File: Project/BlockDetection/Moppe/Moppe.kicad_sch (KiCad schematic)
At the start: 41 parts, among them J1 Conn_01x02_Pin, J2 Conn_01x02_Pin, J3 Conn_01x02_Pin, J4 Conn_01x02_Pin, J5 Conn_01x02_Pin, J6 Conn_01x02_Pin, J7 Amphenol RJHSE5380, J8 Conn_01x02_Pin, Q1 BC856, Q2 BC856 or BC557, Q3 BC856 or BC557, Q4 BC856 or BC557, U1 PC847, U2 PC817

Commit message: tlp620
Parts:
- added D14: S5AC, Diode_THT:D_DO-201AD_P15.24mm_Horizontal, symbol Diode:1N5400
- added D15: 1N5400, Diode_THT:D_DO-201AD_P15.24mm_Horizontal, symbol Diode:1N5400
- added D16, D17: IR26-21C_L110_TR8, LED_SMD:LED_1206_3216Metric, symbol LED:IR26-21C_L110_TR8
- added J9: Conn_01x03_Socket, Package_TO_SOT_THT:TO-92_Inline, symbol Connector:Conn_01x03_Socket
- added Q5: BC557, Package_TO_SOT_SMD:SOT-23, symbol Transistor_BJT:BC856
- added Q6: BC547, Package_TO_SOT_THT:TO-92_Inline, symbol Transistor_BJT:BC547
- added R11: 10R, symbol Device:R
- added R12: 1K8, symbol Device:R
- added U4: TLP620, Package_SO:SOP-4_4.4x2.6mm_P1.27mm, symbol Isolator:TLP290
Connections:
- new net: D17.1 (K), Q6.1 (C)
- new net: Q5.1 (B), Q6.2 (B), R11.1
- new net: D14.2 (A), D15.1 (K), J9.1 (Pin_1), Q5.2 (E), Q6.3 (E)
- new net: R12.1, U4.1
- new net: D16.1 (K), D17.2 (A), R12.2
- new net: J9.3 (Pin_3), U4.2
- new net: D14.1 (K), D15.2 (A), J9.2 (Pin_2), R11.2
- new net: D16.2 (A), Q5.3 (C)

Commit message: efter test
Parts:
- removed C1, C2, C3, C4: 10 µF, symbol Device:C_Polarized_Small
- removed D13: D_Bridge_+-AA, Module:Pololu_Breakout-16_15.2x20.3mm, symbol Device:D_Bridge_+-AA
- removed D14: S5AC, Diode_THT:D_DO-201AD_P15.24mm_Horizontal, symbol Diode:1N5400
- removed D15: 1N5400, Diode_THT:D_DO-201AD_P15.24mm_Horizontal, symbol Diode:1N5400
- removed D16, D17: IR26-21C_L110_TR8, LED_SMD:LED_1206_3216Metric, symbol LED:IR26-21C_L110_TR8
- removed J7: Amphenol RJHSE5380, Connector_RJ:RJ45_Amphenol_RJHSE5380, symbol Connector:RJ45_Shielded
- removed J8: Conn_01x02_Pin, Connector:Tag-Connect_TC2030-IDC-FP_2x03_P1.27mm_Vertical, symbol Connector:Conn_01x02_Pin
- removed J9: Conn_01x03_Socket, Package_TO_SOT_THT:TO-92_Inline, symbol Connector:Conn_01x03_Socket
- removed Q1: BC856, Package_TO_SOT_SMD:SOT-23, symbol Transistor_BJT:BC856
- removed Q2, Q3, Q4: BC856 or BC557, Package_TO_SOT_SMD:SOT-23, symbol Transistor_BJT:BC856
- removed Q5: BC557, Package_TO_SOT_SMD:SOT-23, symbol Transistor_BJT:BC856
- removed Q6: BC547, Package_TO_SOT_THT:TO-92_Inline, symbol Transistor_BJT:BC547
- removed U2: PC817, Package_DIP:DIP-4_W7.62mm, symbol Isolator:PC817
- removed U4: TLP620, Package_SO:SOP-4_4.4x2.6mm_P1.27mm, symbol Isolator:TLP290
- added C1: 100nF, symbol Device:C
- added C2: 10µF, Package_QFP:LQFP-100_14x14mm_P0.5mm, symbol Device:C_Polarized
- added C3: 3,3µF, Package_QFP:LQFP-100_14x14mm_P0.5mm, symbol Device:C_Polarized
- added J7: Conn_01x04_Socket, Connector:Tag-Connect_TC2030-IDC-NL_2x03_P1.27mm_Vertical, symbol Connector:Conn_01x04_Socket
- added Q1, Q2, Q3, Q4: BC557, Package_TO_SOT_THT:TO-92_Inline, symbol Transistor_BJT:BC557
- added U2: MAX485E, Package_SO:SOIC-8_3.9x4.9mm_P1.27mm, symbol Interface_UART:MAX485E
- added U3: ESP32-C3-WROOM-02, RF_Module:ESP32-C3-WROOM-02, symbol RF_Module:ESP32-C3-WROOM-02
- added U4: LT1129-3.3_SOT223, Package_TO_SOT_SMD:SOT-223-3_TabPin2, symbol Regulator_Linear:LT1129-3.3_SOT223
- R10: value 22R -> 4K7; footprint (none) -> Inductor_THT:L_CommonMode_PulseElectronics_PH9455x105NL_1
- R11: value 10R -> 4K7; footprint (none) -> Inductor_THT:L_CommonMode_PulseElectronics_PH9455x105NL_1
- R12: value 1K8 -> 10K; footprint (none) -> Inductor_THT:L_CommonMode_PulseElectronics_PH9455x105NL_1
- R9: value 470R -> 120R; footprint (none) -> Inductor_THT:L_CommonMode_PulseElectronics_PH9455x105NL_1
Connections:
- net at R11.1: now also R9.2, J7.3 (Pin_3), U2.7 (B)
- net GND: now reaches J1.1 (Pin_1), J2.1 (Pin_1), J4.1 (Pin_1), J5.1 (Pin_1), J6.1 (Pin_1), U1.4, U1.6, U1.8
- net GND: no longer J3.1 (Pin_1), U1.2
- net GNDD: now reaches U1.15
- net GNDD: now also R11.2, R12.2, U1.11, U1.13, U1.9, C1.2, C2.2, C3.2, J7.4 (Pin_4), U2.5 (GND), U3.19 (GND), U3.9 (GND), U4.2 (GND)
- net at U1.16: now also U3.18 (IO0)
- net at D2.2 (A), D3.2 (A), D4.2 (A)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: now also Q2.3 (E), Q3.3 (E), Q4.3 (E); no longer D1.2 (A), D5.1 (K), J1.2 (Pin_2), R10.2, R9.1
- net at R12.1: now also U2.2 (~{RE}), U2.3 (DE)
- net at R5.2: now also Q1.1 (C)
- net at R6.2: now also Q2.1 (C)
- net at R2.1: now also Q2.2 (B)
- net at U1.12: now also U3.16 (IO2)
- net at R10.1: now also C1.1, C2.1, C3.1, U2.8 (VCC), U3.1 (3V3), U3.2 (EN), U4.3 (VO)
- net at R7.2: now also Q3.1 (C)
- net at U1.14: now also U3.17 (IO1)
- net at R3.1: now also Q3.2 (B)
- net at R4.1: now also Q4.2 (B)
- net at U1.10: now also U3.15 (IO3)
- net at R8.2: now also Q4.1 (C)
- net at R1.1: now also Q1.2 (B)
- new net: J3.1 (Pin_1), U1.2
- new net: U2.1 (RO), U3.12 (IO21/TXD)
- new net: U2.4 (DI), U3.11 (IO20/RXD)
- new net: J7.2 (Pin_2), R10.2, R9.1, U2.6 (A)
- new net: D1.2 (A), D5.1 (K), J1.2 (Pin_2), Q1.3 (E)
- new net: J7.1 (Pin_1), U4.1 (VI)
- no-connect marks 0 -> 9
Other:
- moved on the sheet: D10, D11, D12, D2, D3, D4, D6, D7, D8, D9, J2, J3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

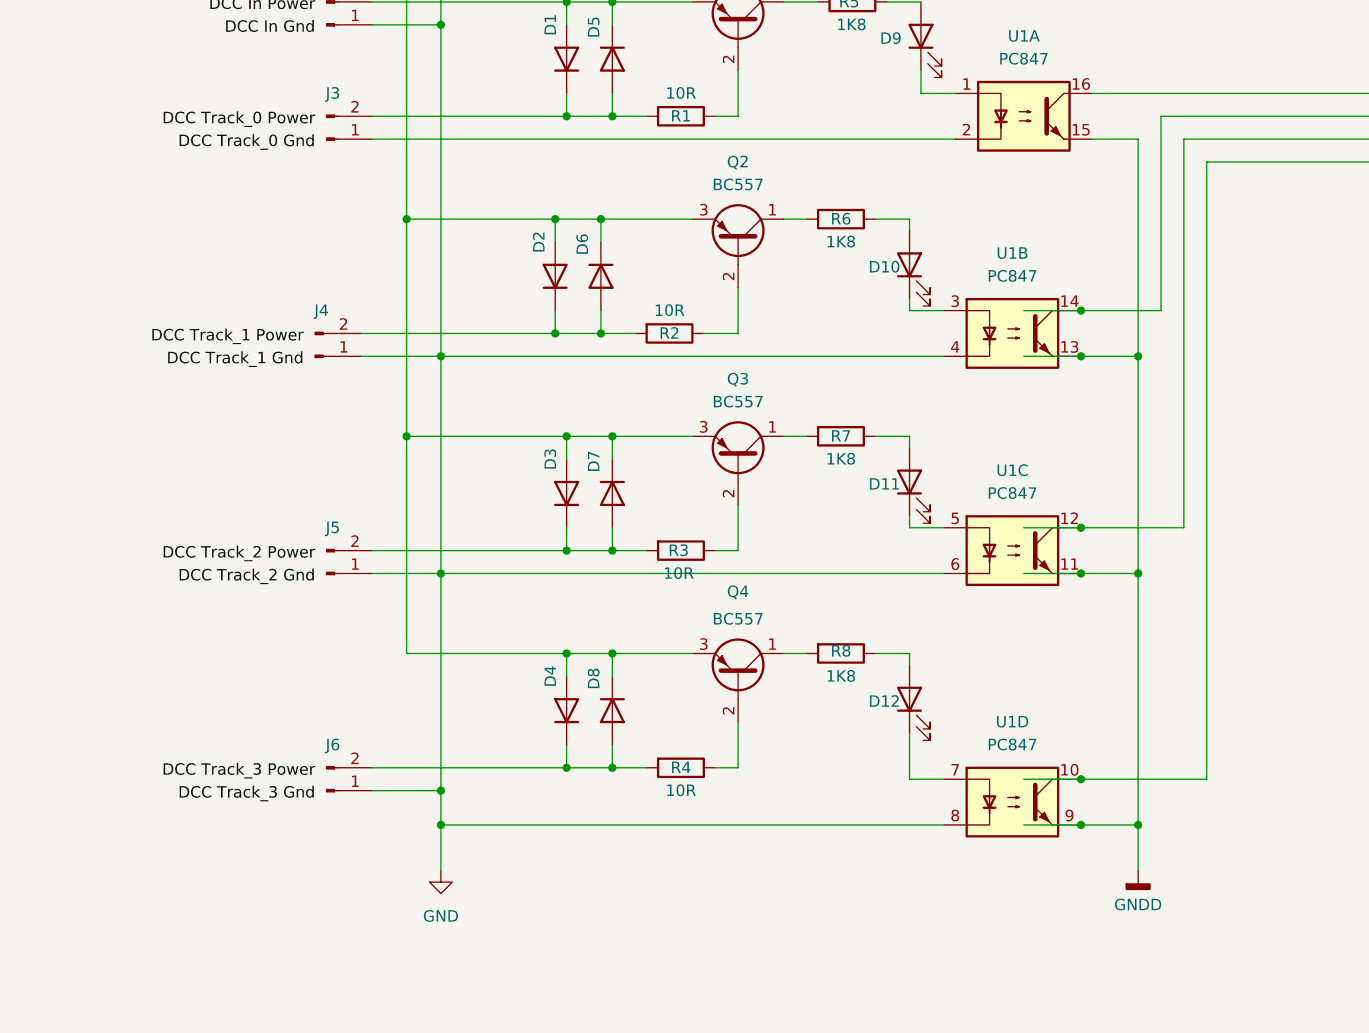
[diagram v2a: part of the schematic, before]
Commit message: AI Help Wifi_On_Off
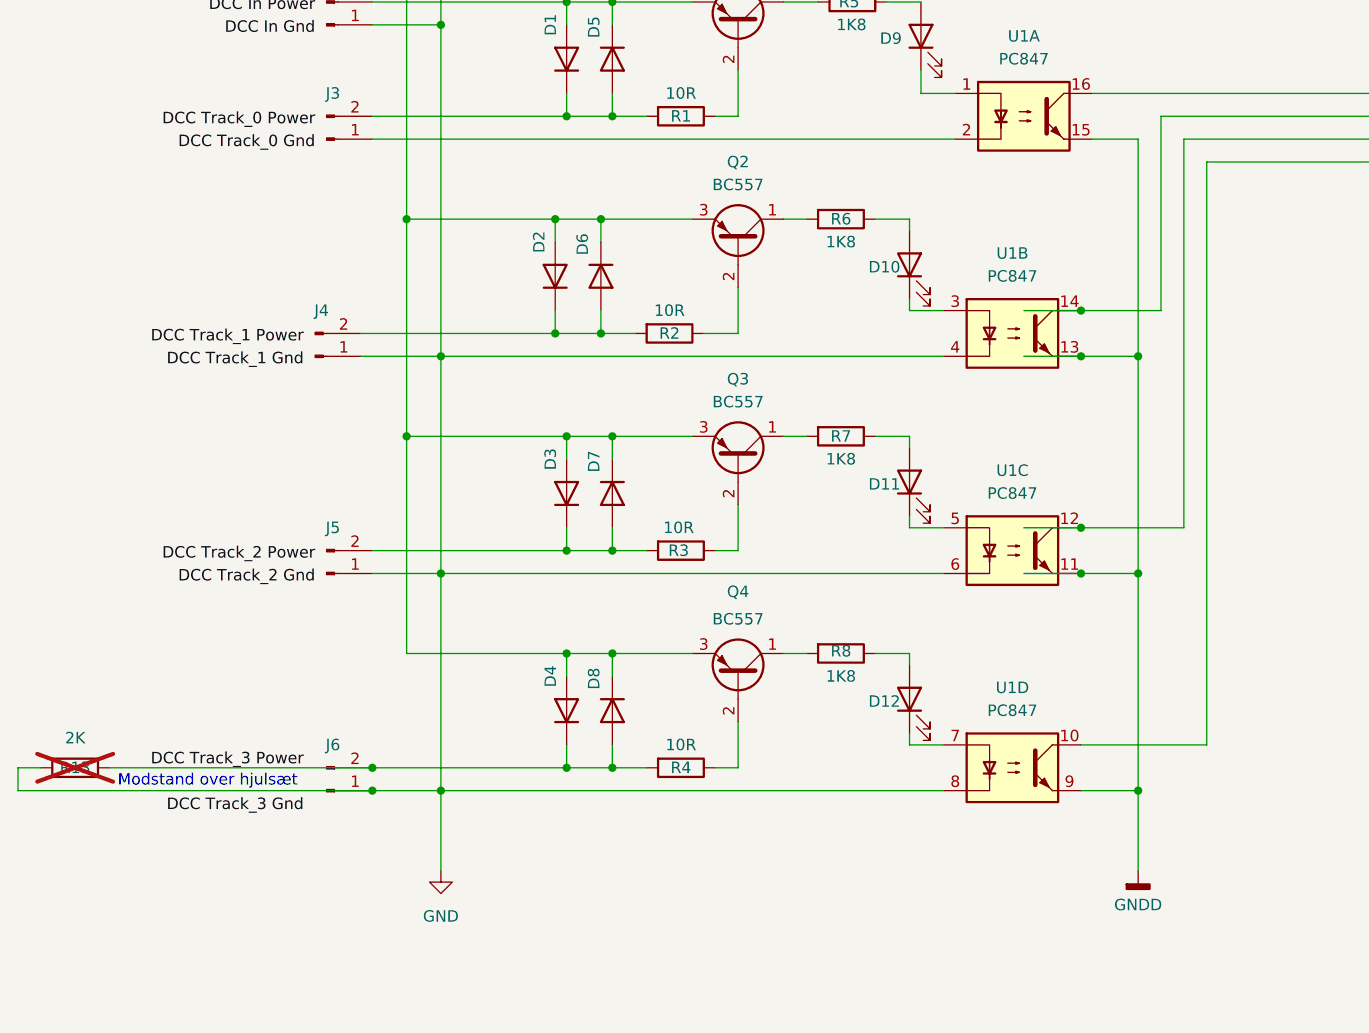
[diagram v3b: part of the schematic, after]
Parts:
- added R13: 2K, symbol Device:R
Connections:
- net DCC Track_3 Power: now also D4.1 (K), D8.2 (A), J6.2 (Pin_2), R4.2, R13.1
- net GND: now also R13.2
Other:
- note added: "Modstand over hjulsæt"
- moved on the sheet: U1D

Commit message: Moppe
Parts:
- added C4, C5, C6, C7: 4;7µF, symbol Device:C_Polarized
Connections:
- net GND: now also C5.2, C6.2, C7.2
- net at D9.1 (K), U1.1: now also C4.1
- net at J3.1 (Pin_1), U1.2: now also C4.2
- net at D11.1 (K), U1.5: now also C6.1
- net at D12.1 (K), U1.7: now also C7.1
- net at D10.1 (K), U1.3: now also C5.1
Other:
- moved on the sheet: D10, D11, D12, D9, R5, U1A, U1B, U1C, U1D

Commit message: SporBesat a la´ Moppe
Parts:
- removed U2: MAX485E, Package_SO:SOIC-8_3.9x4.9mm_P1.27mm, symbol Interface_UART:MAX485E
- added R14, R15: 20K, Inductor_THT:L_CommonMode_PulseElectronics_PH9455x105NL_1, symbol Device:R
- added U5: 4N35, Package_DIP:DIP-6_W7.62mm, symbol Isolator:4N35
- added U6: MAX3485, Package_DIP:DIP-16_W7.62mm, symbol Interface_UART:MAX3485
- C4, C5, C6, C7: value 4;7µF -> 1µF
- R12: value 10K -> 20K
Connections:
- net GNDD: now also U6.5 (GND); no longer R12.2
- net at D9.1 (K), U1.1: no longer C4.1
- net at Q3.1 (C), R7.2: now also C6.1
- net at D11.1 (K), U1.5: no longer C6.1
- net at U3.12 (IO21/TXD): now also R15.2, U6.4 (DI)
- net +3V3: now reaches R12.1
- net +3V3: now also C1.1, C2.1, C3.1, R10.1, U3.1 (3V3), U4.3 (VO), R14.1, R15.1, U6.8 (VCC)
- net at U3.11 (IO20/RXD): now also R12.2, U6.1 (RO)
- net at J7.2 (Pin_2), R10.2, R9.1: now also U6.6 (A)
- net at J7.3 (Pin_3), R11.1, R9.2: now also U6.7 (B)
- net at Q1.1 (C), R5.2: now also C4.1
- net at Q2.1 (C), R6.2: now also C5.1
- net at D12.1 (K), U1.7: no longer C7.1
- net at D10.1 (K), U1.3: no longer C5.1
- net at U3.3 (IO4): now also R14.2, U6.2 (~{RE}), U6.3 (DE)
- net +5V: now reaches J7.1 (Pin_1), U4.1 (VI)
- net at Q4.1 (C), R8.2: now also C7.1
- now unconnected: U3.2 (EN)
- no-connect marks 9 -> 8
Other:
- note added: "For at beregne størrelsen på kondensator C4, C5, C6 & C7, der skal holde strømmen til en LED i 200 mikrosekunder, skal du bruge formlen for elektrisk ladning og strøm: C= (I*t)/(ΔV) Find dine værdier Tid (t): 200 µs = 0,0002 sekunder LED strøm (I): En typisk LED bruger omkring 20 mA, hvilket er 0,02 Ampere. Spændingsfald (Δ V): Det er forskellen på din forsyningsspænding (V_start}) og den mindste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"
- moved on the sheet: C1, C2, C3, C4, C5, C6, C7, D1, D10, D11, D12, D2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

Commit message: Moppe2.svg
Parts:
- removed C4, C5, C6, C7: 1µF, symbol Device:C_Polarized
- added C4, C5, C6, C7: 1µF, symbol Device:C
- added JP1: Jumper_2_Small_Bridged, symbol Jumper:Jumper_2_Small_Bridged
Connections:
- net GND: now also C5.2, C6.2, C7.2
- net at J3.1 (Pin_1), U1.2: now also C4.2
- net at Q3.1 (C), R7.2: now also C6.1
- net at Q1.1 (C), R5.2: now also C4.1
- net at J7.3 (Pin_3), R11.1, U6.7 (B): now also JP1.2 (B); no longer R9.2
- net at Q2.1 (C), R6.2: now also C5.1
- net at Q4.1 (C), R8.2: now also C7.1
- new net: JP1.1 (A), R9.2
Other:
- moved on the sheet: R11

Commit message: moppe rj45
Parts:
- added J8, J9: RJ45, Connector_RJ:RJ45_Amphenol_RJMG1BD3B8K1ANR, symbol Connector:RJ45
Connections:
- net GNDD: now also J8.6, J8.7, J8.8, J9.6, J9.7, J9.8
- net at J7.3 (Pin_3), JP1.2 (B), R11.1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: now also J8.5, J9.5
- net at J7.2 (Pin_2), R10.2, R9.1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: now also J8.4, J9.4
- net +5V renamed +9-30 VDC
- net +9-30 VDC: now also J8.1, J8.2, J9.1, J9.2
- no-connect marks 8 -> 11
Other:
- company: (none) -> Svenn-Erik K. Thomsen
- title: (none) -> Sporbesat detector med Modbus
- moved on the sheet: C1, C2, C3, JP1, R10, R11, R12, R14, R15, R9, U4, U5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

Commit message: Modbus med RJ45 Cat5e Kabel
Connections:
- no-connect marks 11 -> 10
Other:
- note removed: "For at beregne størrelsen på kondensator C4, C5, C6 & C7, der skal holde strømmen til en LED i 200 mikrosekunder, skal du bruge formlen for elektrisk ladning og strøm: C= (I*t)/(ΔV) Find dine værdier Tid (t): 200 µs = 0,0002 sekunder LED strøm (I): En typisk LED bruger omkring 20 mA, hvilket er 0,02 Ampere. Spændingsfald (Δ V): Det er forskellen på din forsyningsspænding (V_start}) og den mindste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"
- moved on the sheet: U5
